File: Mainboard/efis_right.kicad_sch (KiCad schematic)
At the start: 28 parts, among them J23 LB_PULL, J24 LB_PUSH, J25 LB_hPa/inHg, J26 L_FD, J27 L_LS, J28 L_CSTR, J29 L_WPT, J40 L_VORD, J47 L_NDB, J52 L_ARPT, J54 L_MAP_MODE, J55 L_MAP_RANGE, J56 LB_ENC, J57 LVOR/ADF_1, J58 LVOR/ADF_2, U3 CD74HC4067M, U4 CD74HC4067M

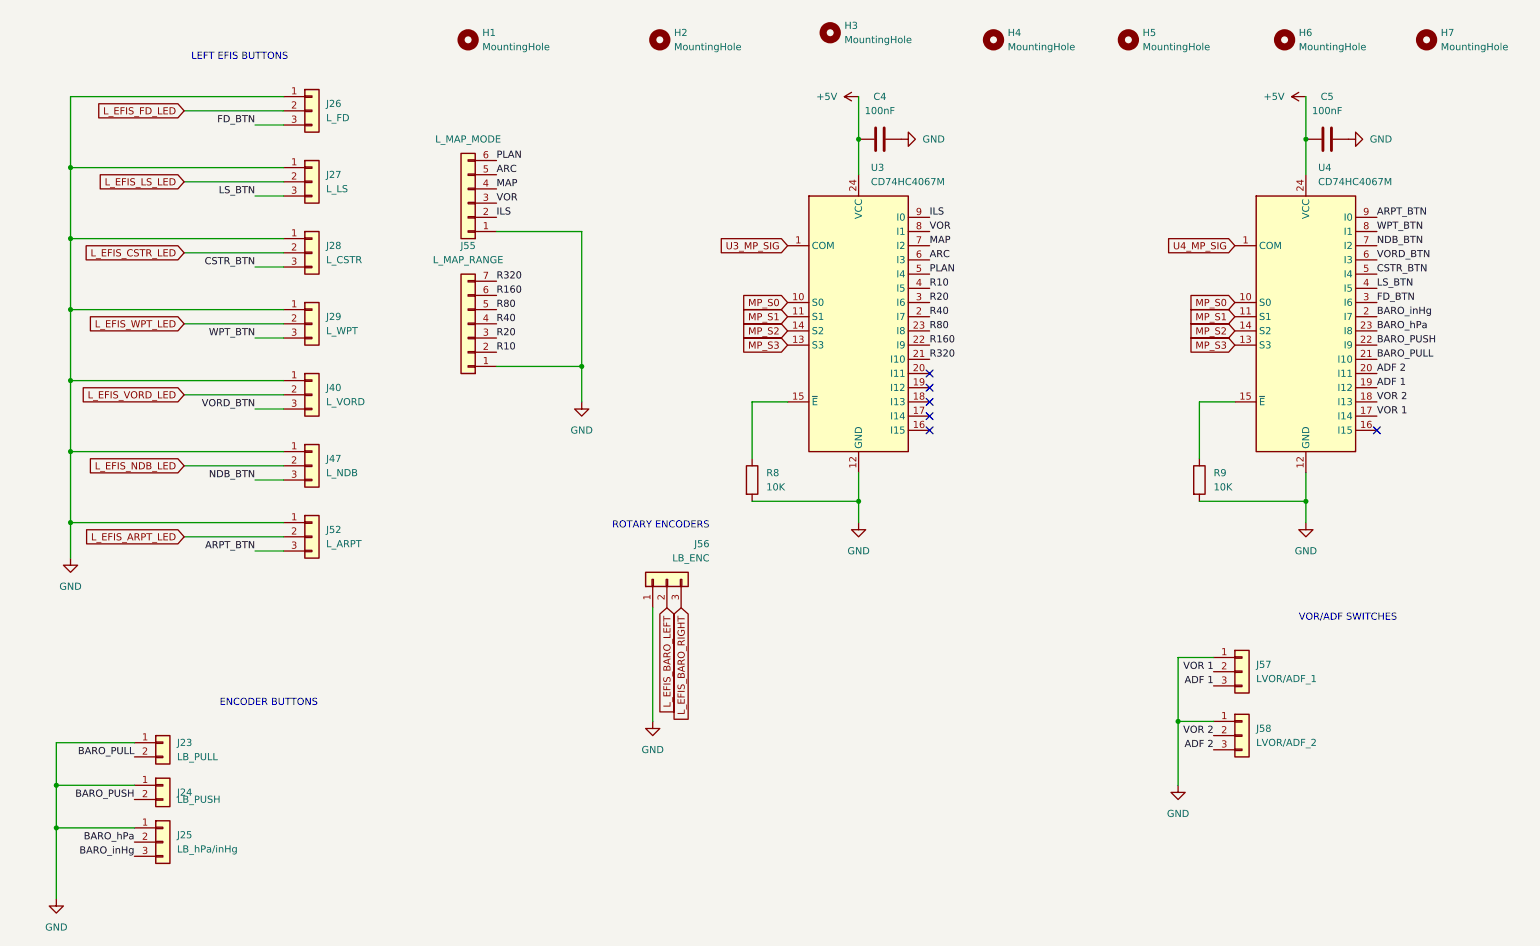
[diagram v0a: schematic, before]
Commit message: Fix the swapped EFIS filenames and rename the backlight nets to +5V
Two naming defects, no electrical change on any board.

EFIS sheets
-----------
The root sheet pointed EFIS_LEFT at efis_right.kicad_sch and EFIS_RIGHT at
efis_left.kicad_sch. The schematic was correct, since the file behind the
LEFT sheet did hold the L_* signals, but the filenames said the opposite and
anyone reading the files from outside KiCad would have been misled.

The two files are swapped and every reference follows: the sheet properties
in the root schematic and the 49 sheetfile entries the footprints carry on
the board. Each file now matches the sheet that loads it.

  netlist   198 nets, 135 components, not one node moved
  ERC       0 violations
  DRC       6 violations, all cosmetic, 0 unconnected, 0 parity issues

Backlight nets
--------------
Every net in the backlighting chain was called +9V while carrying 5 V, on
all four boards. The white LEDs sit behind 91 Ω: at 5 V that is 21 mA, right
at the rating for a 1206 white LED, while 9 V would put them at 65 mA. The
name was a leftover from an earlier design and was the kind of label that
eventually makes someone connect the wrong supply.

Renamed across Korry_Large, Korry_Small, Backlighting_Dimmer and
Backlighting_LEDModule, in both the schematics and the boards: the power
symbol, its value, which is what actually names the net, and the net entries
on the copper. 88 occurrences. None of those boards had a +5V net already,
so nothing was merged.

Verified against the state committed a moment ago: ERC and DRC counts are
identical on all four boards, before and after, and no board gained or lost
a connection.

The Readme drops these two entries and gains the defects that surfaced while
checking: the Backlighting_Dimmer footprints carry their reference in the
value field instead of the schematic value, so a BOM read from that board is
wrong; its terminal block footprint no longer exists in the KiCad library;
four texts on the Korry_Large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
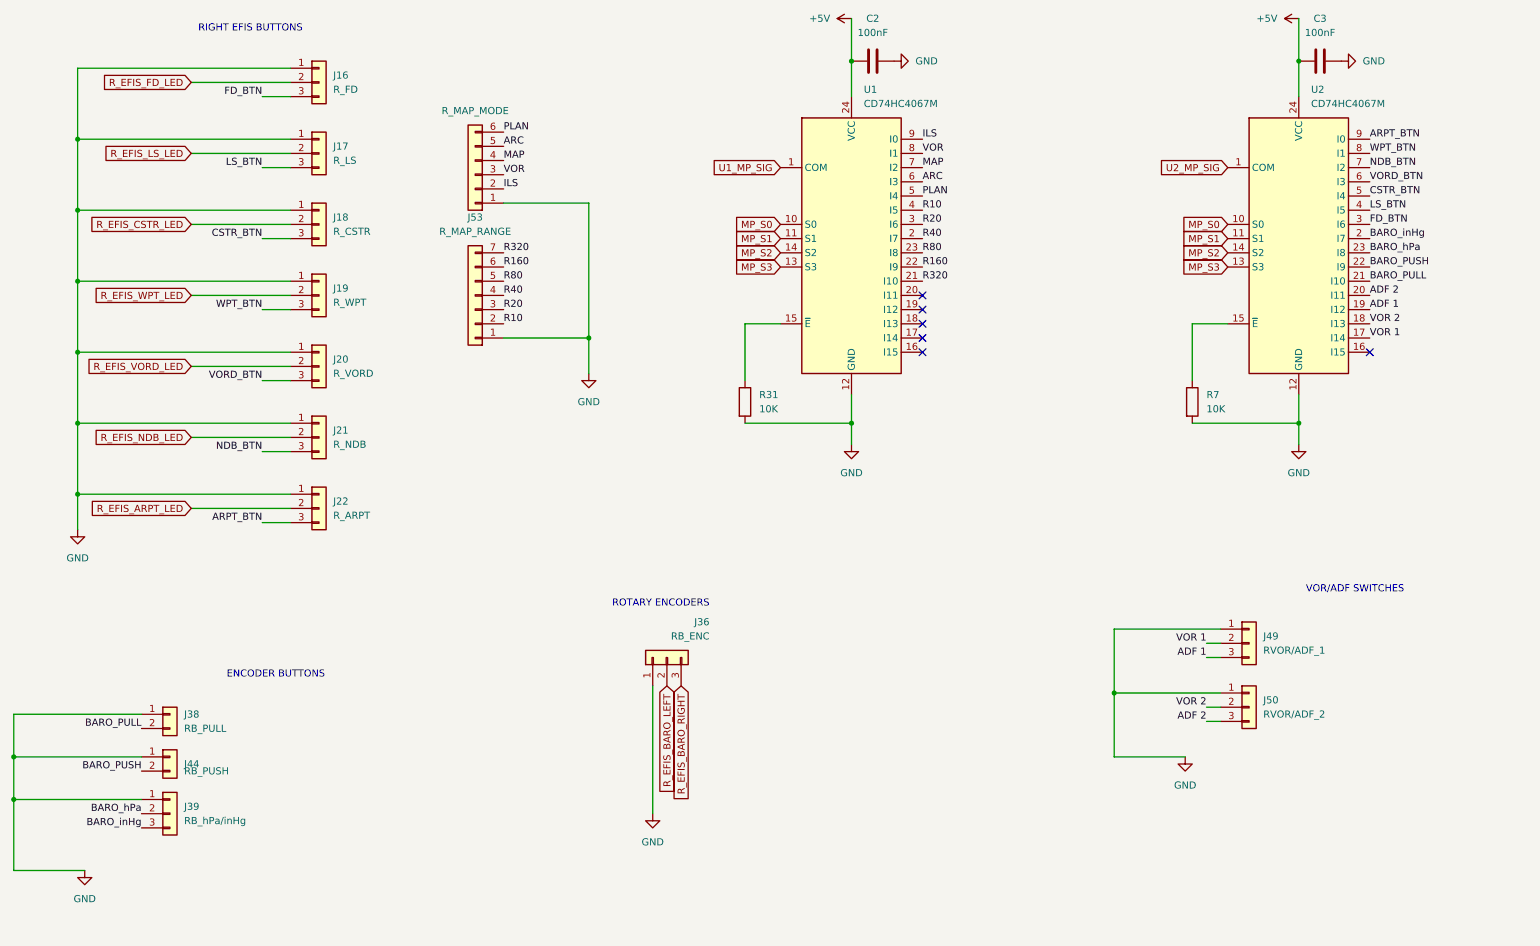
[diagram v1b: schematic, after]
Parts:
- removed C4, C5: 100nF, Capacitor_SMD:C_1206_3216Metric_Pad1.33x1.80mm_HandSolder, symbol Device:C
- removed H1, H2, H3, H4, H5, H6, H7: MountingHole, MountingHole:MountingHole_2.7mm_M2.5_DIN965_Pad_TopBottom, symbol Mechanical:MountingHole
- removed J23: LB_PULL, Connector_PinHeader_2.54mm:PinHeader_1x02_P2.54mm_Vertical, symbol Connector_Generic:Conn_01x02
- removed J24: LB_PUSH, Connector_PinHeader_2.54mm:PinHeader_1x02_P2.54mm_Vertical, symbol Connector_Generic:Conn_01x02
- removed J25: LB_hPa/inHg, Connector_PinHeader_2.54mm:PinHeader_1x03_P2.54mm_Vertical, symbol Connector_Generic:Conn_01x03
- removed J26: L_FD, Connector_PinHeader_2.54mm:PinHeader_1x03_P2.54mm_Vertical, symbol Connector_Generic:Conn_01x03
- removed J27: L_LS, Connector_PinHeader_2.54mm:PinHeader_1x03_P2.54mm_Vertical, symbol Connector_Generic:Conn_01x03
- removed J28: L_CSTR, Connector_PinHeader_2.54mm:PinHeader_1x03_P2.54mm_Vertical, symbol Connector_Generic:Conn_01x03
- removed J29: L_WPT, Connector_PinHeader_2.54mm:PinHeader_1x03_P2.54mm_Vertical, symbol Connector_Generic:Conn_01x03
- removed J40: L_VORD, Connector_PinHeader_2.54mm:PinHeader_1x03_P2.54mm_Vertical, symbol Connector_Generic:Conn_01x03
- removed J47: L_NDB, Connector_PinHeader_2.54mm:PinHeader_1x03_P2.54mm_Vertical, symbol Connector_Generic:Conn_01x03
- removed J52: L_ARPT, Connector_PinHeader_2.54mm:PinHeader_1x03_P2.54mm_Vertical, symbol Connector_Generic:Conn_01x03
- removed J54: L_MAP_MODE, Connector_PinHeader_2.54mm:PinHeader_1x06_P2.54mm_Vertical, symbol Connector_Generic:Conn_01x06
- removed J55: L_MAP_RANGE, Connector_PinHeader_2.54mm:PinHeader_1x07_P2.54mm_Vertical, symbol Connector_Generic:Conn_01x07
- removed J56: LB_ENC, Connector_PinHeader_2.54mm:PinHeader_1x03_P2.54mm_Vertical, symbol Connector_Generic:Conn_01x03
- removed J57: LVOR/ADF_1, Connector_PinHeader_2.54mm:PinHeader_1x03_P2.54mm_Vertical, symbol Connector_Generic:Conn_01x03
- removed J58: LVOR/ADF_2, Connector_PinHeader_2.54mm:PinHeader_1x03_P2.54mm_Vertical, symbol Connector_Generic:Conn_01x03
- removed R8, R9: 10K, Resistor_SMD:R_1206_3216Metric_Pad1.30x1.75mm_HandSolder, symbol Device:R
- removed U3, U4: CD74HC4067M, Package_SO:SOIC-24W_7.5x15.4mm_P1.27mm, symbol 74xx:CD74HC4067M
- added C2, C3: 100nF, Capacitor_SMD:C_1206_3216Metric_Pad1.33x1.80mm_HandSolder, symbol Device:C
- added J16: R_FD, Connector_PinHeader_2.54mm:PinHeader_1x03_P2.54mm_Vertical, symbol Connector_Generic:Conn_01x03
- added J17: R_LS, Connector_PinHeader_2.54mm:PinHeader_1x03_P2.54mm_Vertical, symbol Connector_Generic:Conn_01x03
- added J18: R_CSTR, Connector_PinHeader_2.54mm:PinHeader_1x03_P2.54mm_Vertical, symbol Connector_Generic:Conn_01x03
- added J19: R_WPT, Connector_PinHeader_2.54mm:PinHeader_1x03_P2.54mm_Vertical, symbol Connector_Generic:Conn_01x03
- added J20: R_VORD, Connector_PinHeader_2.54mm:PinHeader_1x03_P2.54mm_Vertical, symbol Connector_Generic:Conn_01x03
- added J21: R_NDB, Connector_PinHeader_2.54mm:PinHeader_1x03_P2.54mm_Vertical, symbol Connector_Generic:Conn_01x03
- added J22: R_ARPT, Connector_PinHeader_2.54mm:PinHeader_1x03_P2.54mm_Vertical, symbol Connector_Generic:Conn_01x03
- added J36: RB_ENC, Connector_PinHeader_2.54mm:PinHeader_1x03_P2.54mm_Vertical, symbol Connector_Generic:Conn_01x03
- added J38: RB_PULL, Connector_PinHeader_2.54mm:PinHeader_1x02_P2.54mm_Vertical, symbol Connector_Generic:Conn_01x02
- added J39: RB_hPa/inHg, Connector_PinHeader_2.54mm:PinHeader_1x03_P2.54mm_Vertical, symbol Connector_Generic:Conn_01x03
- added J44: RB_PUSH, Connector_PinHeader_2.54mm:PinHeader_1x02_P2.54mm_Vertical, symbol Connector_Generic:Conn_01x02
- added J49: RVOR/ADF_1, Connector_PinHeader_2.54mm:PinHeader_1x03_P2.54mm_Vertical, symbol Connector_Generic:Conn_01x03
- added J50: RVOR/ADF_2, Connector_PinHeader_2.54mm:PinHeader_1x03_P2.54mm_Vertical, symbol Connector_Generic:Conn_01x03
- added J51: R_MAP_MODE, Connector_PinHeader_2.54mm:PinHeader_1x06_P2.54mm_Vertical, symbol Connector_Generic:Conn_01x06
- added J53: R_MAP_RANGE, Connector_PinHeader_2.54mm:PinHeader_1x07_P2.54mm_Vertical, symbol Connector_Generic:Conn_01x07
- added R31, R7: 10K, Resistor_SMD:R_1206_3216Metric_Pad1.30x1.75mm_HandSolder, symbol Device:R
- added U1, U2: CD74HC4067M, Package_SO:SOIC-24W_7.5x15.4mm_P1.27mm, symbol 74xx:CD74HC4067M
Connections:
- net +5V: now also C2.1, C3.1, U1.24 (VCC), U2.24 (VCC)
- net ADF 1: now also J49.3 (Pin_3), U2.19 (I12)
- net ADF 2: now also J50.3 (Pin_3), U2.20 (I11)
- net ARC: now also J51.5 (Pin_5), U1.6 (I3)
- net ARPT_BTN: now also J22.3 (Pin_3), U2.9 (I0)
- net BARO_PULL: now also J38.2 (Pin_2), U2.21 (I10)
- net BARO_PUSH: now also J44.2 (Pin_2), U2.22 (I9)
- net BARO_hPa: now also J39.2 (Pin_2), U2.23 (I8)
- net BARO_inHg: now also J39.3 (Pin_3), U2.2 (I7)
- net CSTR_BTN: now also J18.3 (Pin_3), U2.5 (I4)
- net FD_BTN: now also J16.3 (Pin_3), U2.3 (I6)
- net GND: now also C2.2, C3.2, J16.1 (Pin_1), J17.1 (Pin_1), J18.1 (Pin_1), J19.1 (Pin_1), J20.1 (Pin_1), J21.1 (Pin_1), J22.1 (Pin_1), J36.1 (Pin_1), J38.1 (Pin_1), J39.1 (Pin_1), J44.1 (Pin_1), J49.1 (Pin_1), J50.1 (Pin_1), J51.1 (Pin_1), J53.1 (Pin_1), R31.2, R7.2, U1.12 (GND), U2.12 (GND)
- net ILS: now also J51.2 (Pin_2), U1.9 (I0)
- net LS_BTN: now also J17.3 (Pin_3), U2.4 (I5)
- net MAP: now also J51.4 (Pin_4), U1.7 (I2)
- net MP_S0: now also U1.10 (S0), U2.10 (S0)
- net MP_S1: now also U1.11 (S1), U2.11 (S1)
- net MP_S2: now also U1.14 (S2), U2.14 (S2)
- net MP_S3: now also U1.13 (S3), U2.13 (S3)
- net NDB_BTN: now also J21.3 (Pin_3), U2.7 (I2)
- net PLAN: now also J51.6 (Pin_6), U1.5 (I4)
- net R10: now also J53.2 (Pin_2), U1.4 (I5)
- net R160: now also J53.6 (Pin_6), U1.22 (I9)
- net R20: now also J53.3 (Pin_3), U1.3 (I6)
- net R320: now also J53.7 (Pin_7), U1.21 (I10)
- net R40: now also J53.4 (Pin_4), U1.2 (I7)
- net R80: now also J53.5 (Pin_5), U1.23 (I8)
- net VOR: now also J51.3 (Pin_3), U1.8 (I1)
- net VOR 1: now also J49.2 (Pin_2), U2.17 (I14)
- net VOR 2: now also J50.2 (Pin_2), U2.18 (I13)
- net VORD_BTN: now also J20.3 (Pin_3), U2.6 (I3)
- net WPT_BTN: now also J19.3 (Pin_3), U2.8 (I1)
- new net: R31.1, U1.15 (~{E})
- new net: R7.1, U2.15 (~{E})
- new net R_EFIS_ARPT_LED: J22.2 (Pin_2)
- new net R_EFIS_BARO_LEFT: J36.2 (Pin_2)
- new net R_EFIS_BARO_RIGHT: J36.3 (Pin_3)
- new net R_EFIS_CSTR_LED: J18.2 (Pin_2)
- new net R_EFIS_FD_LED: J16.2 (Pin_2)
- new net R_EFIS_LS_LED: J17.2 (Pin_2)
- new net R_EFIS_NDB_LED: J21.2 (Pin_2)
- new net R_EFIS_VORD_LED: J20.2 (Pin_2)
- new net R_EFIS_WPT_LED: J19.2 (Pin_2)
- new net U1_MP_SIG: U1.1 (COM)
- new net U2_MP_SIG: U2.1 (COM)
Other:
- note added: "RIGHT EFIS BUTTONS"
- note removed: "LEFT EFIS BUTTONS"
